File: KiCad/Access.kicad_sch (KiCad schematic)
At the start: 66 parts, among them J1 USB-C, J2 RFID, J3 INPUTS, J4 ExtTamper, J5 POWER, J6 DOOR, Q1 NX7002AK, SW1 Tamper, U1 ESP32-WROOM-32, U2 FT231XQ, U3 G3VM-41GR8, U4 LMR16006+FB, U5 LMR16006+FB, U6 AA, U7 QR

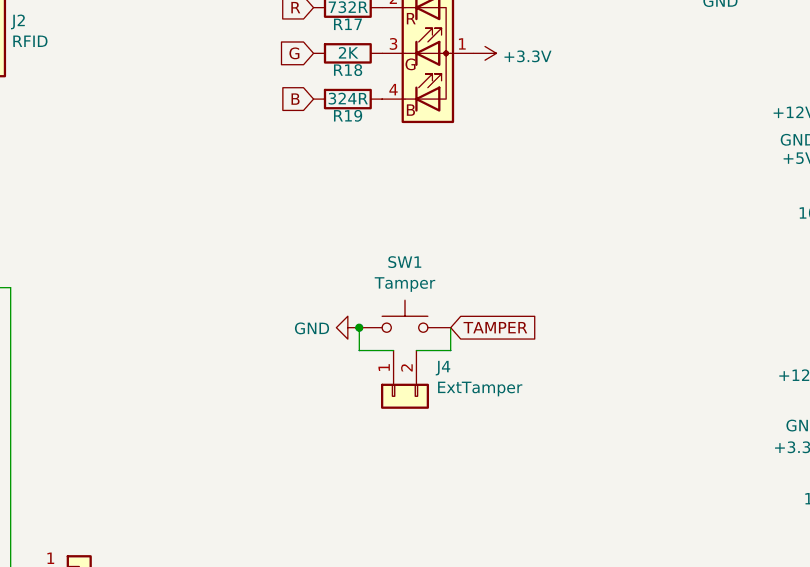
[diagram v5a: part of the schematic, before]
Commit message: New tamper switch
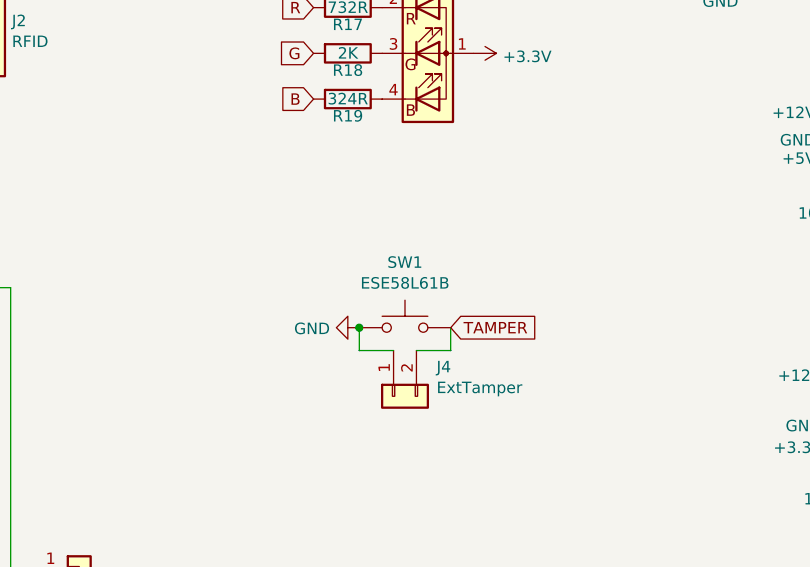
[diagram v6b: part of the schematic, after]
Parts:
- J4: footprint TestPoint:TestPoint_2Pads_Pitch5.08mm_Drill1.3mm -> Connector_PinHeader_2.54mm:PinHeader_1x02_P2.54mm_Vertical
- SW1: value Tamper -> ESE58L61B; footprint RevK:SW_PUSH_6mm_SMD -> RevK:ESE58
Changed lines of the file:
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@@
     (in_bom yes) (on_board yes)
     (property "Reference" "SW1" (id 0) (at 183.515 104.521 0))
-    (property "Value" "Tamper" (id 1) (at 183.515 106.8324 0))
-    (property "Footprint" "RevK:SW_PUSH_6mm_SMD" (id 2) (at 183.515 106.68 0)
-      (effects (font (size 1.27 1.27)) hide)
-    )
-    (property "Datasheet" "~" (id 3) (at 183.515 106.68 0)
+    (property "Value" "ESE58L61B" (id 1) (at 183.515 106.8324 0))
+    (property "Footprint" "RevK:ESE58" (id 2) (at 183.515 106.68 0)
+      (effects (font (size 1.27 1.27)) hide)
+    )
+    (property "Datasheet" "https://docs.rs-online.com/3c26/0900766b810ad108.pdf" (id 3) (at 183.515 106.68 0)
       (effects (font (size 1.27 1.27)) hide)
     )
@@
       (effects (font (size 1.27 1.27)) (justify right))
     )
-    (property "Footprint" "TestPoint:TestPoint_2Pads_Pitch5.08mm_Drill1.3mm" (id 2) (at 182.245 119.38 0)
+    (property "Footprint" "Connector_PinHeader_2.54mm:PinHeader_1x02_P2.54mm_Vertical" (id 2) (at 182.245 119.38 0)
       (effects (font (size 1.27 1.27)) hide)
     )
@@
     (pin "2")
     (pin "6")
+    (pin "3")
+    (pin "4")
+    (pin "5")
   )
   (symbol (lib_id "Device:R") (at 117.475 107.315 270) (unit 1)
@@
     (pin "2")
     (pin "6")
+    (pin "3")
+    (pin "4")
+    (pin "5")
   )
   (symbol (lib_id "power:+3.3V") (at 113.665 102.235 0) (unit 1)
@@
       (effects (font (size 1.27 1.27)) hide)
     )
+    (pin "1")
+    (pin "2")
+    (pin "6")
     (pin "3")
     (pin "4")
@@
       (effects (font (size 1.27 1.27)) hide)
     )
+    (pin "1")
+    (pin "2")
+    (pin "6")
     (pin "3")
     (pin "4")
@@
     (pin "2")
     (pin "6")
+    (pin "3")
+    (pin "4")
+    (pin "5")
   )
   (symbol (lib_id "power:+3.3V") (at 113.665 132.715 0) (unit 1)
@@
       (effects (font (size 1.27 1.27)) hide)
     )
+    (pin "1")
+    (pin "2")
+    (pin "6")
     (pin "3")
     (pin "4")
@@
     (pin "2")
     (pin "6")
+    (pin "3")
+    (pin "4")
+    (pin "5")
   )
   (symbol (lib_id "power:+3.3V") (at 114.3 163.195 0) (unit 1)
@@
       (effects (font (size 1.27 1.27)) hide)
     )
+    (pin "1")
+    (pin "2")
+    (pin "6")
     (pin "3")
     (pin "4")
@@
     )
     (path "/00000000-0000-0000-0000-00006094f3ad"
-      (reference "J4") (unit 1) (value "ExtTamper") (footprint "TestPoint:TestPoint_2Pads_Pitch5.08mm_Drill1.3mm")
+      (reference "J4") (unit 1) (value "ExtTamper") (footprint "Connector_PinHeader_2.54mm:PinHeader_1x02_P2.54mm_Vertical")
     )
     (path "/00000000-0000-0000-0000-00006074263f"
@@
     )
     (path "/00000000-0000-0000-0000-00006093be97"
-      (reference "SW1") (unit 1) (value "Tamper") (footprint "RevK:SW_PUSH_6mm_SMD")
+      (reference "SW1") (unit 1) (value "ESE58L61B") (footprint "RevK:ESE58")
     )
     (path "/a64e4ded-c775-489a-9996-ddd97aa3988a"

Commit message: Revised tamper
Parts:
- SW1: value ESE58L61B -> ESE13V01D; footprint RevK:ESE58 -> RevK:ESE13
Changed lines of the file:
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@@
     (in_bom yes) (on_board yes)
     (property "Reference" "SW1" (id 0) (at 183.515 104.521 0))
-    (property "Value" "ESE58L61B" (id 1) (at 183.515 106.8324 0))
-    (property "Footprint" "RevK:ESE58" (id 2) (at 183.515 106.68 0)
-      (effects (font (size 1.27 1.27)) hide)
-    )
-    (property "Datasheet" "https://docs.rs-online.com/3c26/0900766b810ad108.pdf" (id 3) (at 183.515 106.68 0)
+    (property "Value" "ESE13V01D" (id 1) (at 183.515 106.8324 0))
+    (property "Footprint" "RevK:ESE13" (id 2) (at 183.515 106.68 0)
+      (effects (font (size 1.27 1.27)) hide)
+    )
+    (property "Datasheet" "https://docs.rs-online.com/73f9/0900766b810acfc9.pdf" (id 3) (at 183.515 106.68 0)
       (effects (font (size 1.27 1.27)) hide)
     )
@@
     )
     (path "/00000000-0000-0000-0000-00006093be97"
-      (reference "SW1") (unit 1) (value "ESE58L61B") (footprint "RevK:ESE58")
+      (reference "SW1") (unit 1) (value "ESE13V01D") (footprint "RevK:ESE13")
     )
     (path "/a64e4ded-c775-489a-9996-ddd97aa3988a"
